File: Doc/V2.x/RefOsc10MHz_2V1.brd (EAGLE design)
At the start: 90 x 70 mm, 82 parts, among them CON1 TYCO-AMP_USBUSB-B_SMT, CON2 HEADER-2X5SMD, CON3 SD-73100-0105, CON4 AVR-ISP-6SMD, CON5 AVR-JTAG-10SMD, CON6 HEADER-2X3SMD, CON7 MCX-J-P-X-RA-SM1, IC1 ATmega328-P, IC2 LC4032V_XXT44, IC3 74HCT221D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

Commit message: avr_DF4IAH_Bootloader - Doc - Eagle: V2.1 - correction: CRS80 --> CRS08 (2)
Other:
- board text added: "DF4IAH 10 MHz Ref.-Osc. V 2.1a"
- board text removed: "DF4IAH 10 MHz Ref.-Osc. V 2.1"
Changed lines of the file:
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@@
 <text x="75.940734375" y="65.306415625" size="1.27" layer="26" font="vector" ratio="18" distance="61" rot="MR0" align="center-left">DF4IAH
 10 MHz Ref.-Osc.
-V 2.1</text>
+V 2.1a</text>
 <text x="6.35" y="10.16" size="1.27" layer="16" font="vector" ratio="20" distance="40" rot="MR0">Bot</text>
 <text x="2.54" y="10.16" size="1.27" layer="1" font="vector" ratio="20" distance="40">Top</text>

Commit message: avr_DF4IAH_Bootloader - Doc - Eagle: V2.1/V2.2 - removed elkos and replaced it by C0805 MLCCs
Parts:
- C151, C211, C612, C613: device rcl:PANASONIC_B -> rcl:C0805
- C911: device rcl:PANASONIC_C -> rcl:C0805
- moved C911 1.27 mm to (24.1, 19.1), turned to 0 degrees
- turned C151 to 180 degrees
- turned C211 to 0 degrees
- turned C612 to 0 degrees
- turned C613 to 0 degrees
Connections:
- net +3V3: now also C612.1, C613.1; no longer C612.+, C613.+
- net GND: now also C151.2, C211.2, C612.2, C613.2, C911.2; no longer C151.-, C211.-, C612.-, C613.-, C911.-
- net N_ADC_PULL: now also C151.1; no longer C151.+
- net VCC: now also C211.1, C911.1; no longer C211.+, C911.+
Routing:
- net VCC: track 297.4 -> 293.9 mm
- net GND: track 306.0 -> 303.7 mm
- net N_ADC_PULL: track 74.3 -> 76.3 mm

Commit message: avr_DF4IAH_Bootloader - Doc - Eagle: 2.1, 2.2, 2.3 - three resistors changed
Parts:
- R311: value 4.7k -> 4.3k
- R611: value 10k -> 15k
- R612: value 45.3k -> 68k
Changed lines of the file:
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@@
 <attribute name="VALUE" x="30.48" y="16.51" size="1.016" layer="27"/>
 </element>
-<element name="R612" library="rcl" package="R0805" value="45.3k" x="46.99" y="40.64" smashed="yes" rot="MR0">
+<element name="R612" library="rcl" package="R0805" value="68k" x="46.99" y="40.64" smashed="yes" rot="MR0">
 <attribute name="NAME" x="45.007865625" y="39.54715625" size="1.016" layer="26" rot="MR180"/>
 <attribute name="VALUE" x="44.79206875" y="42.89283125" size="1.016" layer="28" rot="MR180"/>
 </element>
-<element name="R611" library="rcl" package="R0805" value="10k" x="48.26" y="46.99" smashed="yes" rot="MR90">
+<element name="R611" library="rcl" package="R0805" value="15k" x="48.26" y="46.99" smashed="yes" rot="MR90">
 <attribute name="NAME" x="49.2640875" y="45.7731" size="1.016" layer="26" rot="MR90"/>
 <attribute name="VALUE" x="47.568125" y="48.503196875" size="1.016" layer="28" rot="MR90"/>
@@
 <attribute name="VALUE" x="33.287240625" y="43.547825" size="1.016" layer="27" rot="R90"/>
 </element>
-<element name="R311" library="rcl" package="R0805" value="4.7k" x="20.32" y="11.43" smashed="yes" rot="MR0">
+<element name="R311" library="rcl" package="R0805" value="4.3k" x="20.32" y="11.43" smashed="yes" rot="MR0">
 <attribute name="NAME" x="25.05265625" y="10.7852375" size="1.016" layer="26" rot="MR0"/>
 <attribute name="VALUE" x="18.59439375" y="10.671171875" size="1.016" layer="28" rot="MR0"/>

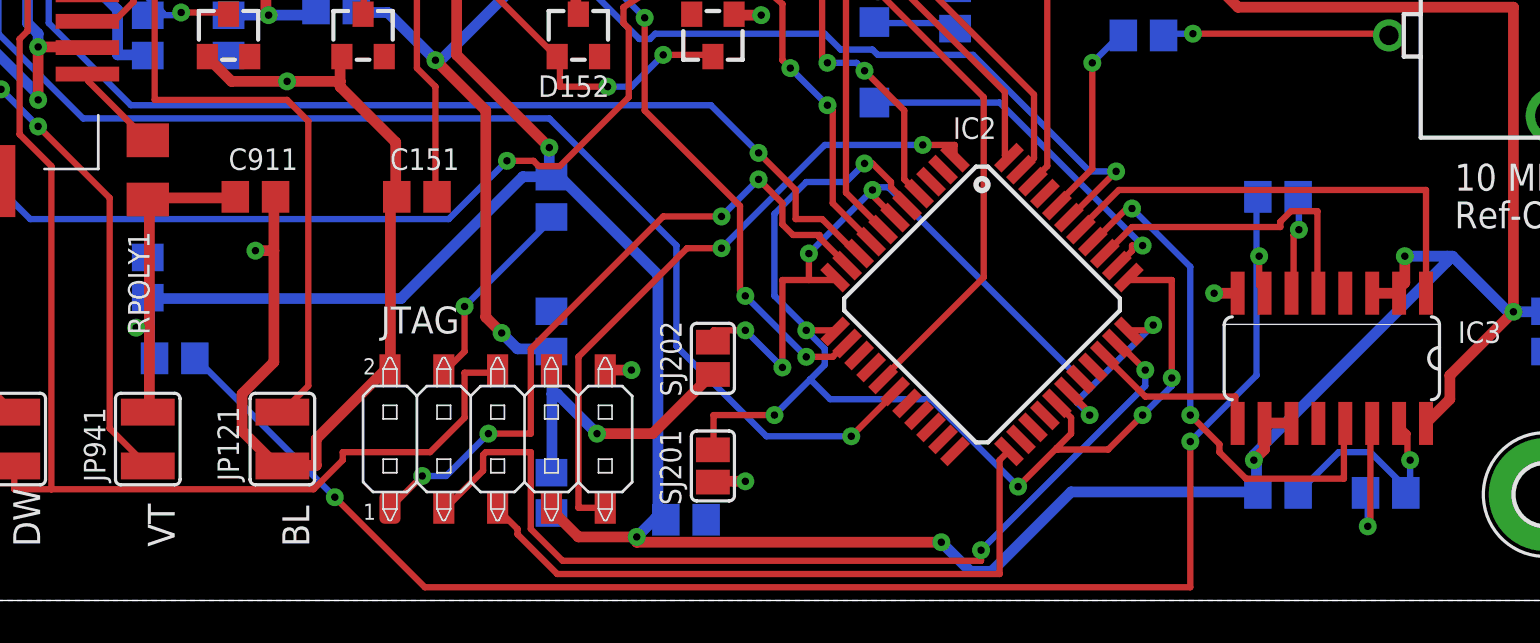
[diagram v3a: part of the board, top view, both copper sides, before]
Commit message: avr_DF4IAH_Bootloader - Doc - Eagle: 2.1, 2.2, 2.3 - misplaced R311 fixed (making short at BL jumper)
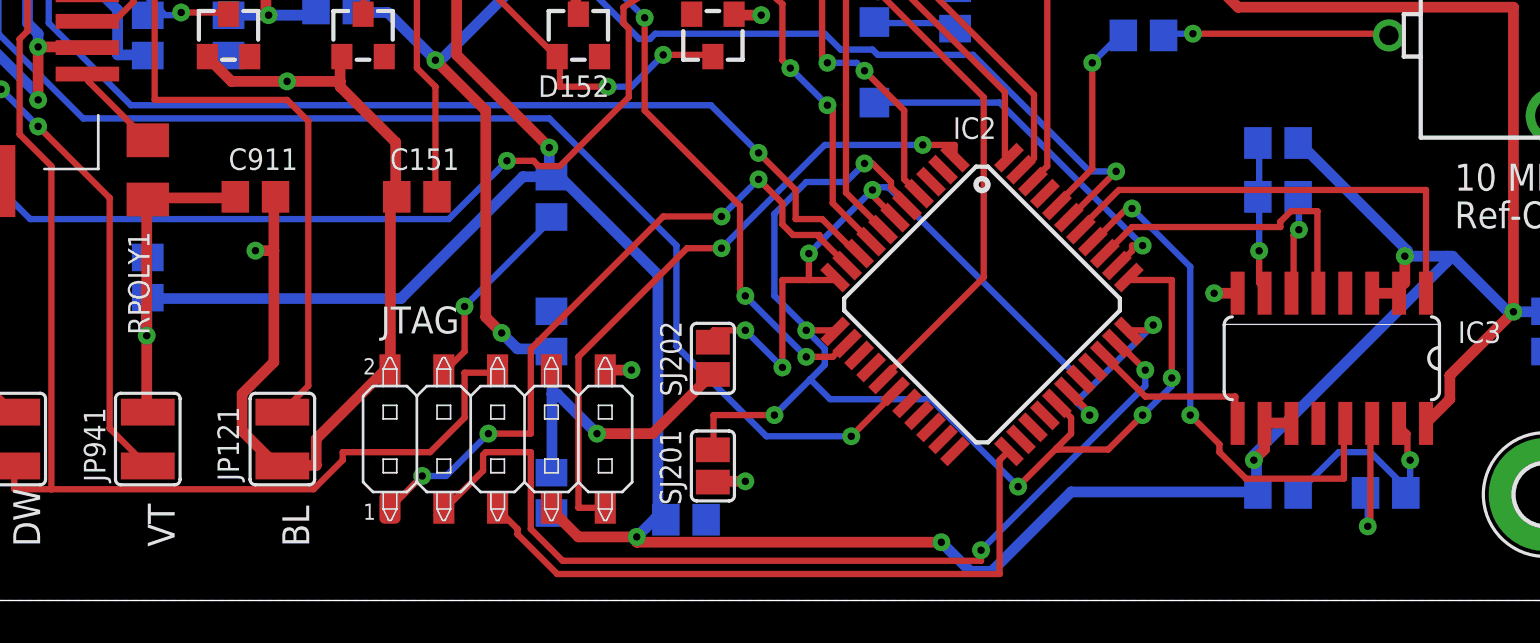
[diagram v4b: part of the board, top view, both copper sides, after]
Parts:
- moved R311 53.1 mm to (72.4, 21.6), turned to 180 degrees
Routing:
- net N$44: track 73.2 -> 7.20 mm, vias 3 -> 1
- net VCC: track 293.9 -> 298.9 mm
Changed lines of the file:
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@@
 <attribute name="VALUE" x="33.287240625" y="43.547825" size="1.016" layer="27" rot="R90"/>
 </element>
-<element name="R311" library="rcl" package="R0805" value="4.3k" x="20.32" y="11.43" smashed="yes" rot="MR0">
-<attribute name="NAME" x="25.05265625" y="10.7852375" size="1.016" layer="26" rot="MR0"/>
-<attribute name="VALUE" x="18.59439375" y="10.671171875" size="1.016" layer="28" rot="MR0"/>
+<element name="R311" library="rcl" package="R0805" value="4.3k" x="72.39" y="21.59" smashed="yes" rot="MR180">
+<attribute name="NAME" x="74.66464375" y="21.9141" size="1.016" layer="26" rot="MR180"/>
+<attribute name="VALUE" x="66.963821875" y="21.9150125" size="1.016" layer="28" rot="MR180"/>
 </element>
 <element name="C612" library="rcl" package="C0805" value="22uF" x="43.18" y="39.37" smashed="yes">
@@
 <wire x1="83.5" y1="28" x2="70.5" y2="28" width="0.508" layer="1"/>
 <wire x1="83.5" y1="13.625" x2="83.5" y2="28" width="0.508" layer="1"/>
-<wire x1="19.125" y1="11.625" x2="19.125" y2="12.875" width="0.508" layer="16"/>
-<wire x1="19.125" y1="12.875" x2="19.125" y2="14.25" width="0.508" layer="16"/>
-<wire x1="19.25" y1="11.5" x2="19.125" y2="11.625" width="0.508" layer="16"/>
-<wire x1="19.125" y1="14.25" x2="19.05" y2="14.29" width="0.508" layer="16"/>
-<wire x1="19.25" y1="11.5" x2="19.37" y2="11.43" width="0.508" layer="16"/>
 <wire x1="19.125" y1="19" x2="19.05" y2="18.92" width="0.508" layer="1"/>
-<wire x1="19.125" y1="18.75" x2="19.125" y2="12.875" width="0.508" layer="1"/>
-<wire x1="19.125" y1="12.875" x2="19.125" y2="9" width="0.508" layer="1"/>
-<wire x1="19.125" y1="9" x2="19.05" y2="8.89" width="0.508" layer="1"/>
-<wire x1="19.125" y1="18.75" x2="19.05" y2="18.92" width="0.508" layer="1"/>
-<wire x1="18.5" y1="12.875" x2="19.125" y2="12.875" width="0.508" layer="16"/>
-<wire x1="19.125" y1="12.875" x2="18.5" y2="12.875" width="0.508" layer="1"/>
 <wire x1="41.75" y1="50" x2="42.125" y2="49.625" width="0.508" layer="1"/>
 <wire x1="41.75" y1="53.25" x2="41.75" y2="50" width="0.508" layer="1"/>
@@
 <via x="83.5" y="13.625" extent="1-16" drill="0.35"/>
 <via x="78.375" y="16.25" extent="1-16" drill="0.35"/>
-<via x="18.5" y="12.875" extent="1-16" drill="0.35"/>
 <via x="39.75" y="58.125" extent="1-16" drill="0.35"/>
 <via x="42.125" y="3" extent="1-16" drill="0.35"/>
@@
 <wire x1="41.5" y1="54.625" x2="42.125" y2="54.625" width="0.508" layer="1"/>
 <wire x1="42.125" y1="54.625" x2="42.23" y2="54.61" width="0.508" layer="1"/>
+<wire x1="78.5" y1="16.5" x2="73.5" y2="21.5" width="0.508" layer="16"/>
+<wire x1="73.5" y1="21.5" x2="73.34" y2="21.59" width="0.508" layer="16"/>
+<wire x1="78.5" y1="16.5" x2="78.375" y2="16.25" width="0.508" layer="16"/>
+<wire x1="19" y1="18.5" x2="19" y2="12.5" width="0.508" layer="1"/>
+<wire x1="19" y1="12.5" x2="19" y2="9" width="0.508" layer="1"/>
+<wire x1="19" y1="9" x2="19.05" y2="8.89" width="0.508" layer="1"/>
+<wire x1="19" y1="18.5" x2="19.05" y2="18.92" width="0.508" layer="1"/>
+<wire x1="19" y1="12.5" x2="19" y2="14" width="0.508" layer="16"/>
+<wire x1="19" y1="14" x2="19.05" y2="14.29" width="0.508" layer="16"/>
+<via x="19" y="12.5" extent="1-16" drill="0.35"/>
 </signal>
 <signal name="N_ADC_PULL">
@@
 <contactref element="C311" pad="2"/>
 <contactref element="R311" pad="1"/>
-<wire x1="27.875" y1="4.875" x2="21.375" y2="11.375" width="0.3" layer="16"/>
-<wire x1="32.125" y1="0.625" x2="27.875" y2="4.875" width="0.3" layer="1"/>
-<wire x1="68.25" y1="0.625" x2="32.125" y2="0.625" width="0.3" layer="1"/>
-<wire x1="68.25" y1="7.5" x2="68.25" y2="0.625" width="0.3" layer="1"/>
-<wire x1="71.375" y1="10.625" x2="68.25" y2="7.5" width="0.3" layer="16"/>
-<wire x1="71.375" y1="19" x2="71.375" y2="16.25" width="0.3" layer="16"/>
-<wire x1="71.375" y1="16.25" x2="71.375" y2="10.625" width="0.3" layer="16"/>
-<wire x1="21.375" y1="11.375" x2="21.27" y2="11.43" width="0.3" layer="16"/>
-<wire x1="71.375" y1="19" x2="71.44" y2="19.05" width="0.3" layer="16"/>
-<wire x1="71.5" y1="14.875" x2="71.75" y2="14.625" width="0.3" layer="1"/>
-<wire x1="71.5" y1="16.25" x2="71.5" y2="14.875" width="0.3" layer="1"/>
-<wire x1="71.75" y1="14.625" x2="71.755" y2="14.5034" width="0.3" layer="1"/>
-<wire x1="71.5" y1="16.25" x2="71.375" y2="16.25" width="0.3" layer="16"/>
-<via x="27.875" y="4.875" extent="1-16" drill="0.35"/>
-<via x="68.25" y="7.5" extent="1-16" drill="0.35"/>
-<via x="71.5" y="16.25" extent="1-16" drill="0.35"/>
+<wire x1="71.5" y1="21.5" x2="71.5" y2="19.5" width="0.3" layer="16"/>
+<wire x1="71.5" y1="19.5" x2="71.44" y2="19.05" width="0.3" layer="16"/>
+<wire x1="71.5" y1="21.5" x2="71.44" y2="21.59" width="0.3" layer="16"/>
+<wire x1="71.5" y1="16.5" x2="71.5" y2="15" width="0.3" layer="1"/>
+<wire x1="71.5" y1="19" x2="71.5" y2="16.5" width="0.3" layer="16"/>
+<wire x1="71.5" y1="15" x2="71.755" y2="14.5034" width="0.3" layer="1"/>
+<wire x1="71.5" y1="19" x2="71.44" y2="19.05" width="0.3" layer="16"/>
+<via x="71.5" y="16.5" extent="1-16" drill="0.35"/>
 </signal>
 <signal name="N$45">
